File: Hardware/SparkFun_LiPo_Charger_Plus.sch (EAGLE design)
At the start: 26 parts, among them U1 MCP73833

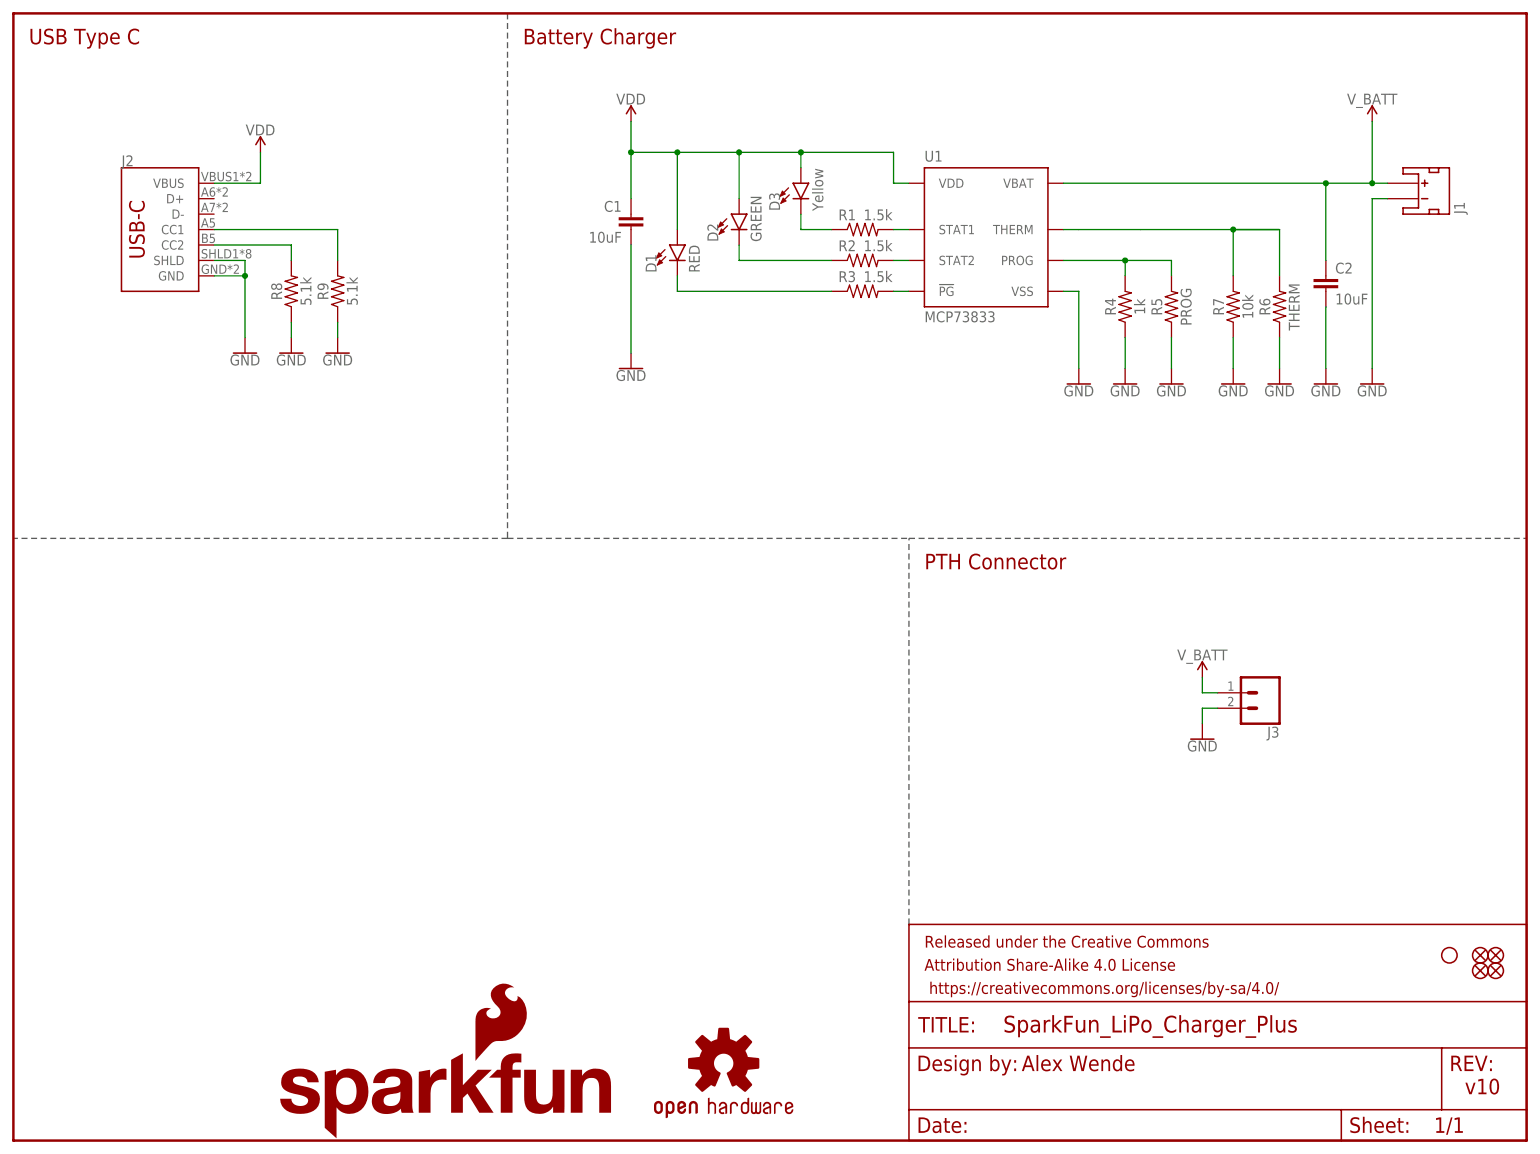
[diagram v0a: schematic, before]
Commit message: v10 Update
Added PROD_ID to U1, fixed part number ordering.
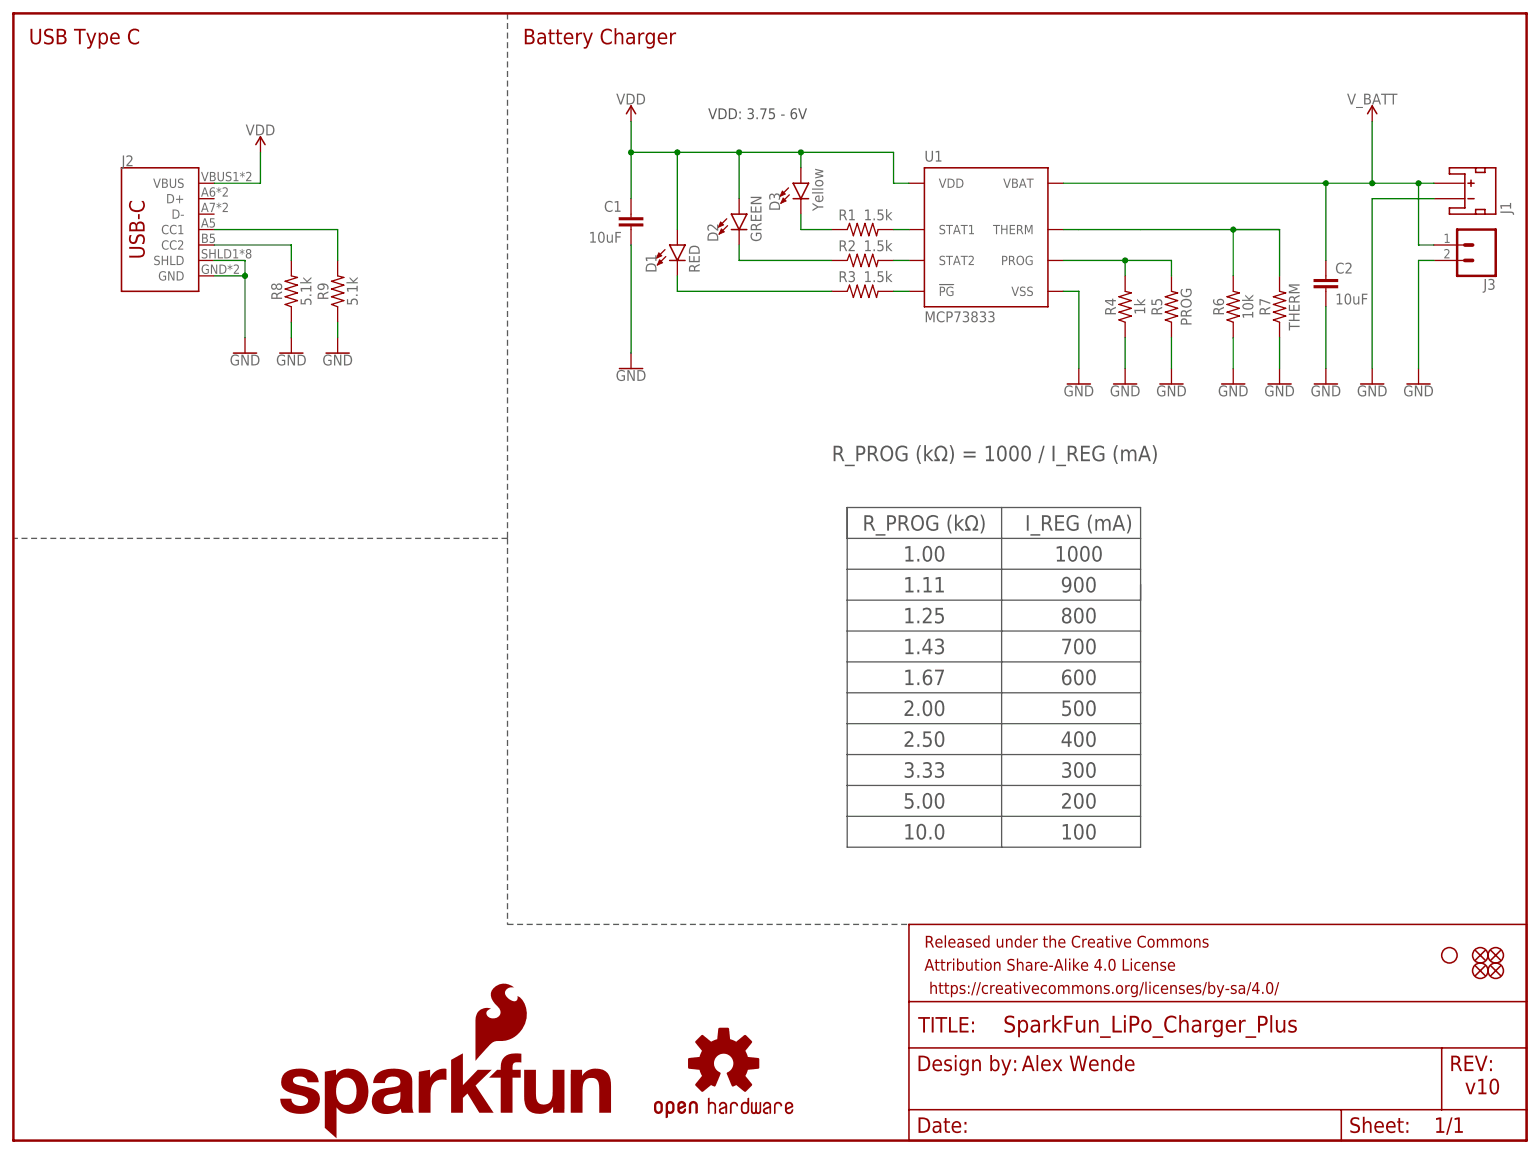
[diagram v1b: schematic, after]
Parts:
- R6: value THERM -> 10k; device SparkFun-Resistors:RESISTORAXIAL-0.3 -> SparkFun-Resistors:10KOHM-0603-1/10W-1%
- R7: value 10k -> THERM; device SparkFun-Resistors:10KOHM-0603-1/10W-1% -> SparkFun-Resistors:RESISTORAXIAL-0.3
- U1: device SparkFun-IC-Power:MCP73833T -> SparkFun-IC-Power:MCP73833
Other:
- note added: "1.00"
- note added: "1.11"
- note added: "1.25"
- note added: "1.43"
- note added: "1.67"
- note added: "10.0"
- note added: "100"
- note added: "1000"
- note added: "2.00"
- note added: "2.50"
- note added: "200"
- note added: "3.33"
- note added: "300"
- note added: "400"
- note added: "5.00"
- note added: "500"
- note added: "600"
- note added: "700"
- note added: "800"
- note added: "900"
- note added: "I_REG (mA)"
- note added: "R_PROG (kΩ)"
- note added: "R_PROG (kΩ) = 1000 / I_REG (mA)"
- note added: "VDD: 3.75 - 6V"
- note removed: "PTH Connector"
- moved on the sheet: J1, J3, R6, R7
